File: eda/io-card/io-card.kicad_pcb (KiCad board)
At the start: 2 copper layers, 158 x 95 mm, 63 parts, among them J2 Bus expansion, J3 PortA, J4 PortB, J5 ControlLines, J6 SPI, J7 Keyboard connector, J8 SD-Card module, J9 SD_Card, U1 W65C22SxP, U10 74HCT193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

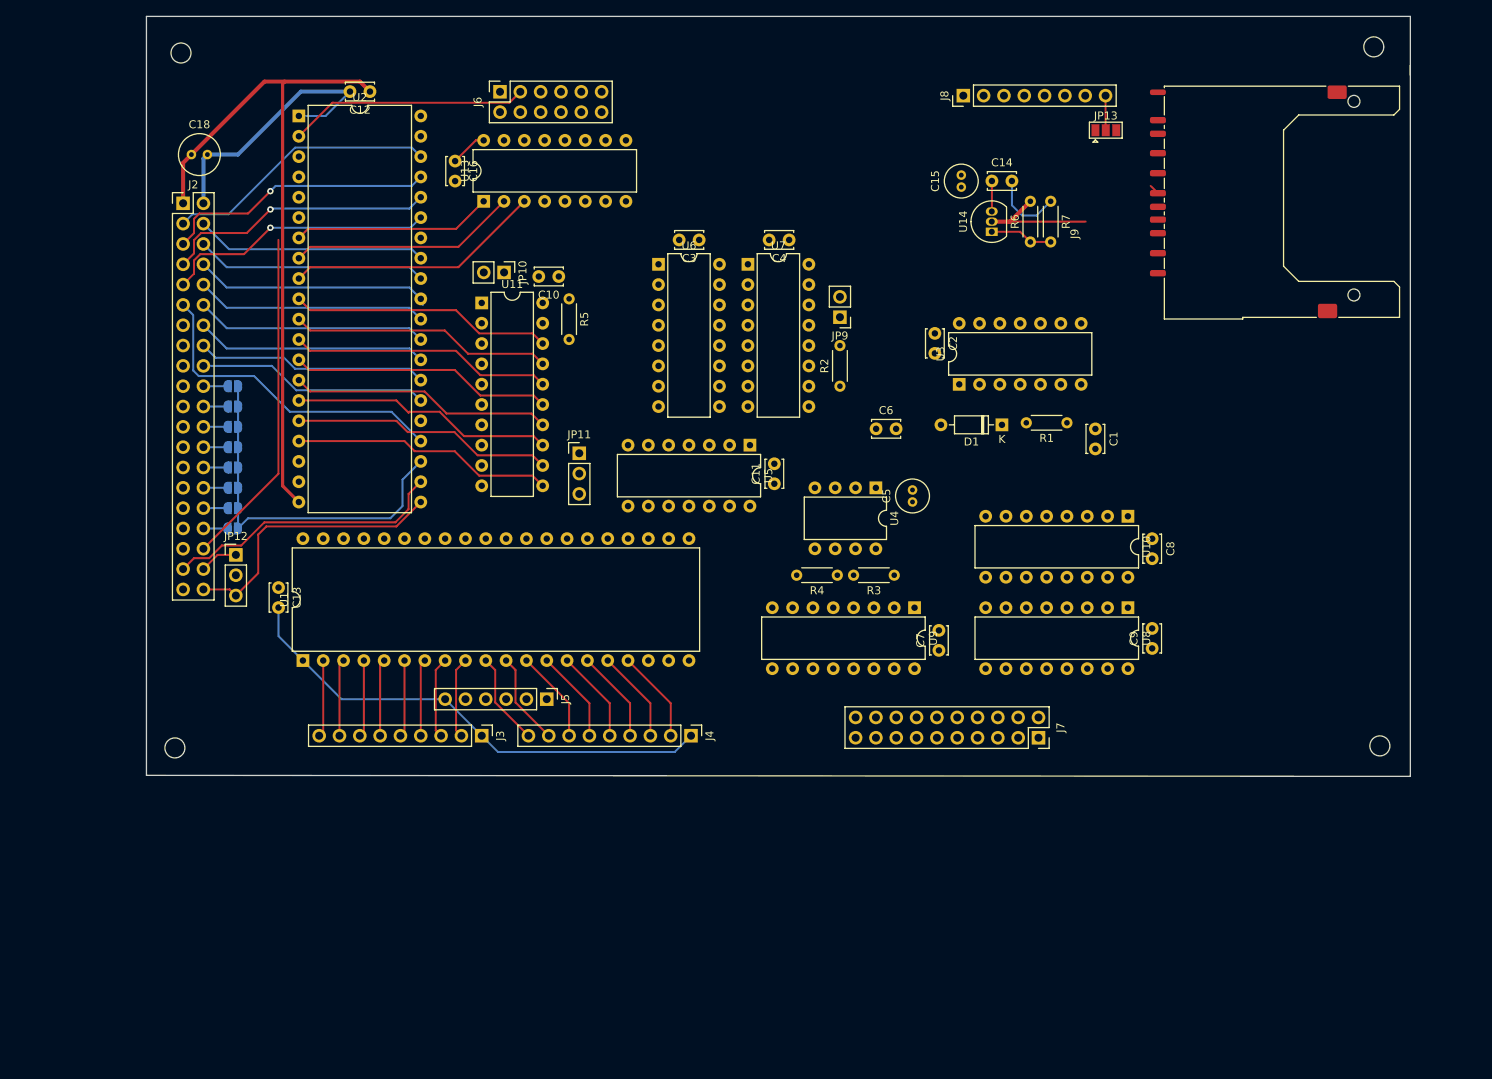
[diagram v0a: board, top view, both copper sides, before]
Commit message: Add skeleton stuff to io-card and gpu
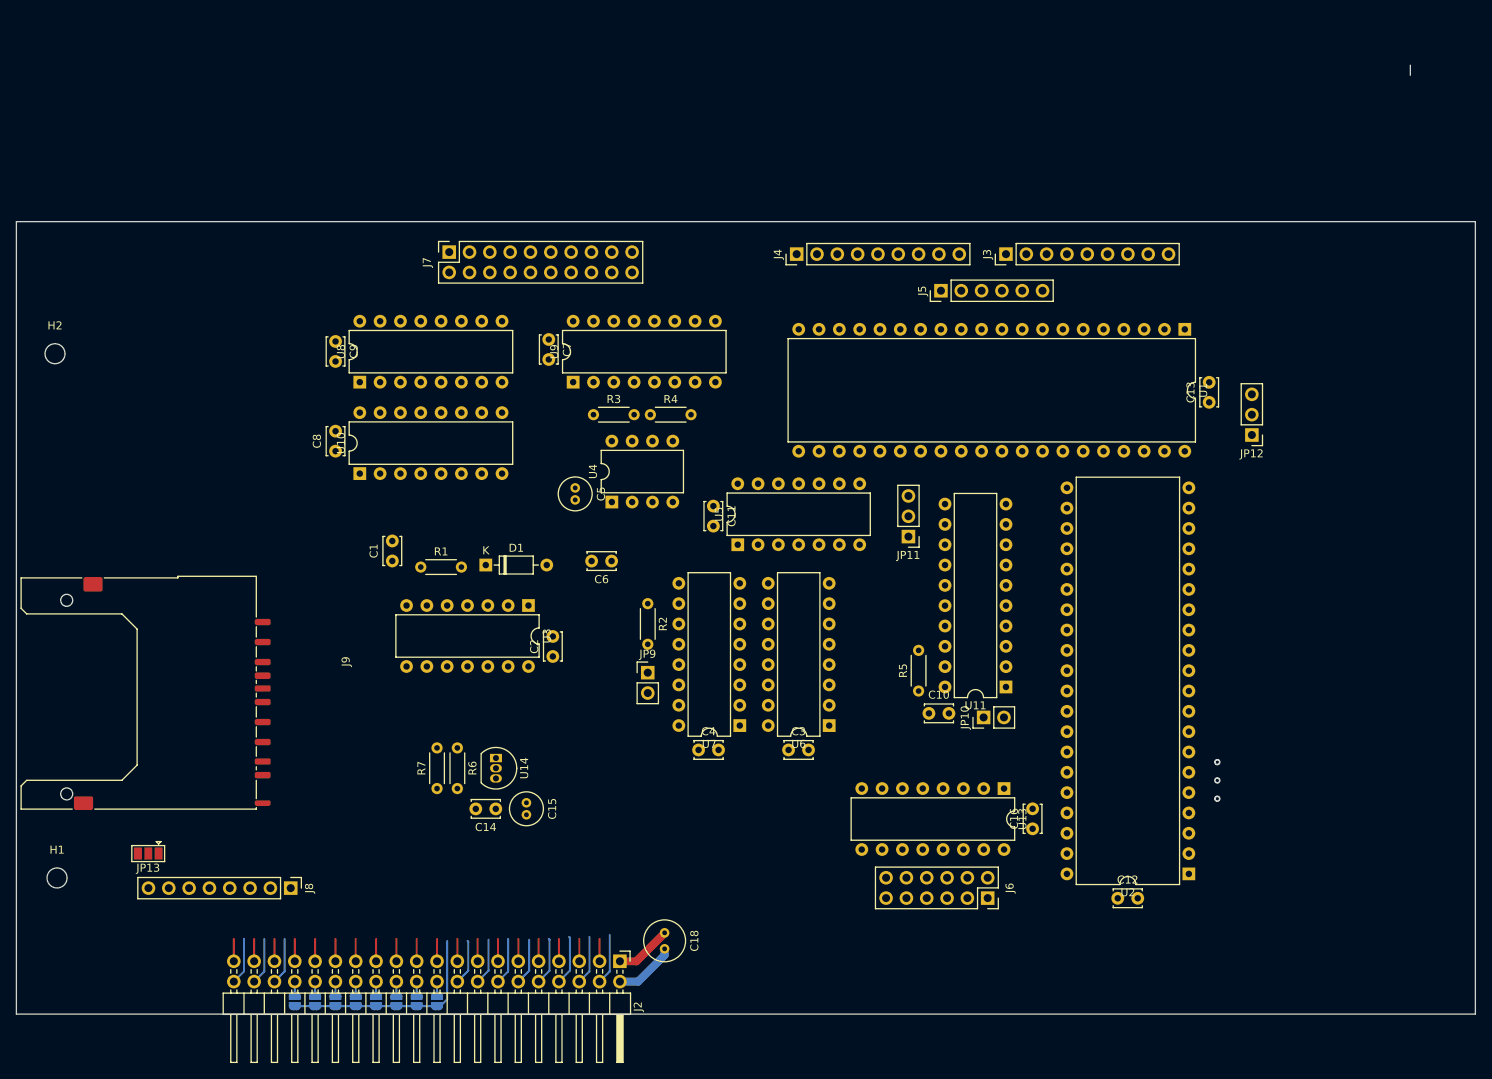
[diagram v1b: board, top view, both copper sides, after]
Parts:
- removed H3, H4: MountingHole, MountingHole:MountingHole_2.5mm
- J2: footprint Connector_PinHeader_2.54mm:PinHeader_2x20_P2.54mm_Vertical -> Connector_PinHeader_2.54mm:PinHeader_2x20_P2.54mm_Horizontal
- moved H2 169.2 mm to (42.4, 71.9)
- moved J9 150.4 mm to (55.9, 114.8), turned to -90 degrees
- moved JP13 150.0 mm to (54.1, 134.4), turned to 180 degrees
- moved U2 146.1 mm to (184.2, 136.9), turned to 180 degrees
- moved C12 137.5 mm to (175.3, 140.0), turned to 0 degrees
- moved J8 129.9 mm to (71.9, 138.7), turned to -90 degrees
- moved JP12 127.9 mm to (192.0, 82.0), turned to 180 degrees
- moved C13 118.6 mm to (186.7, 78.0), turned to 90 degrees
- moved J6 117.8 mm to (159.0, 139.9), turned to -90 degrees
- moved U1 117.8 mm to (183.6, 68.8), turned to -90 degrees
- moved C18 113.9 mm to (118.6, 144.3), turned to -90 degrees
- moved C16 110.4 mm to (164.6, 131.3), turned to 90 degrees
- moved J2 109.4 mm to (113.0, 147.8), turned to -90 degrees
- moved C9 109.1 mm to (77.5, 70.3), turned to -90 degrees
- moved R7 106.2 mm to (90.2, 126.2), turned to 90 degrees
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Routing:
- net GND: track 106.2 -> 7.72 mm
- net VCC: track 95.1 -> 7.05 mm
- net /Expansion header/A4: track 40.8 -> 2.79 mm
- net /~{RST}: track 42.5 -> 5.86 mm
- net /PS2 keyboard interface/KeyboardBit5: track 32.9 -> 0.00 mm
- net /PS2 keyboard interface/KeyboardBit6: track 32.8 -> 0.00 mm
- net /PS2 keyboard interface/KeyboardBit1: track 32.8 -> 0.00 mm
- net /PS2 keyboard interface/KeyboardBit4: track 32.8 -> 0.00 mm
- net /PS2 keyboard interface/KeyboardBit3: track 32.8 -> 0.00 mm
- net /PS2 keyboard interface/KeyboardBit0: track 32.8 -> 0.00 mm
- net /PS2 keyboard interface/KeyboardBit7: track 32.8 -> 0.00 mm
- net /PS2 keyboard interface/KeyboardBit2: track 32.8 -> 0.00 mm
- net /R~{W}: track 35.3 -> 2.79 mm
- net Net-(U13-A2): track 32.2 -> 0.00 mm
- net /Expansion header/A2: track 34.4 -> 2.79 mm
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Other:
- board size 158 x 95 mm -> 182.4 x 118.6 mm
- board text added: "0"
- board text added: "1"
- board text added: "2"
- board text added: "3"
- board text added: "4"
- board text added: "5"
- board text added: "6"
- board text added: "7"

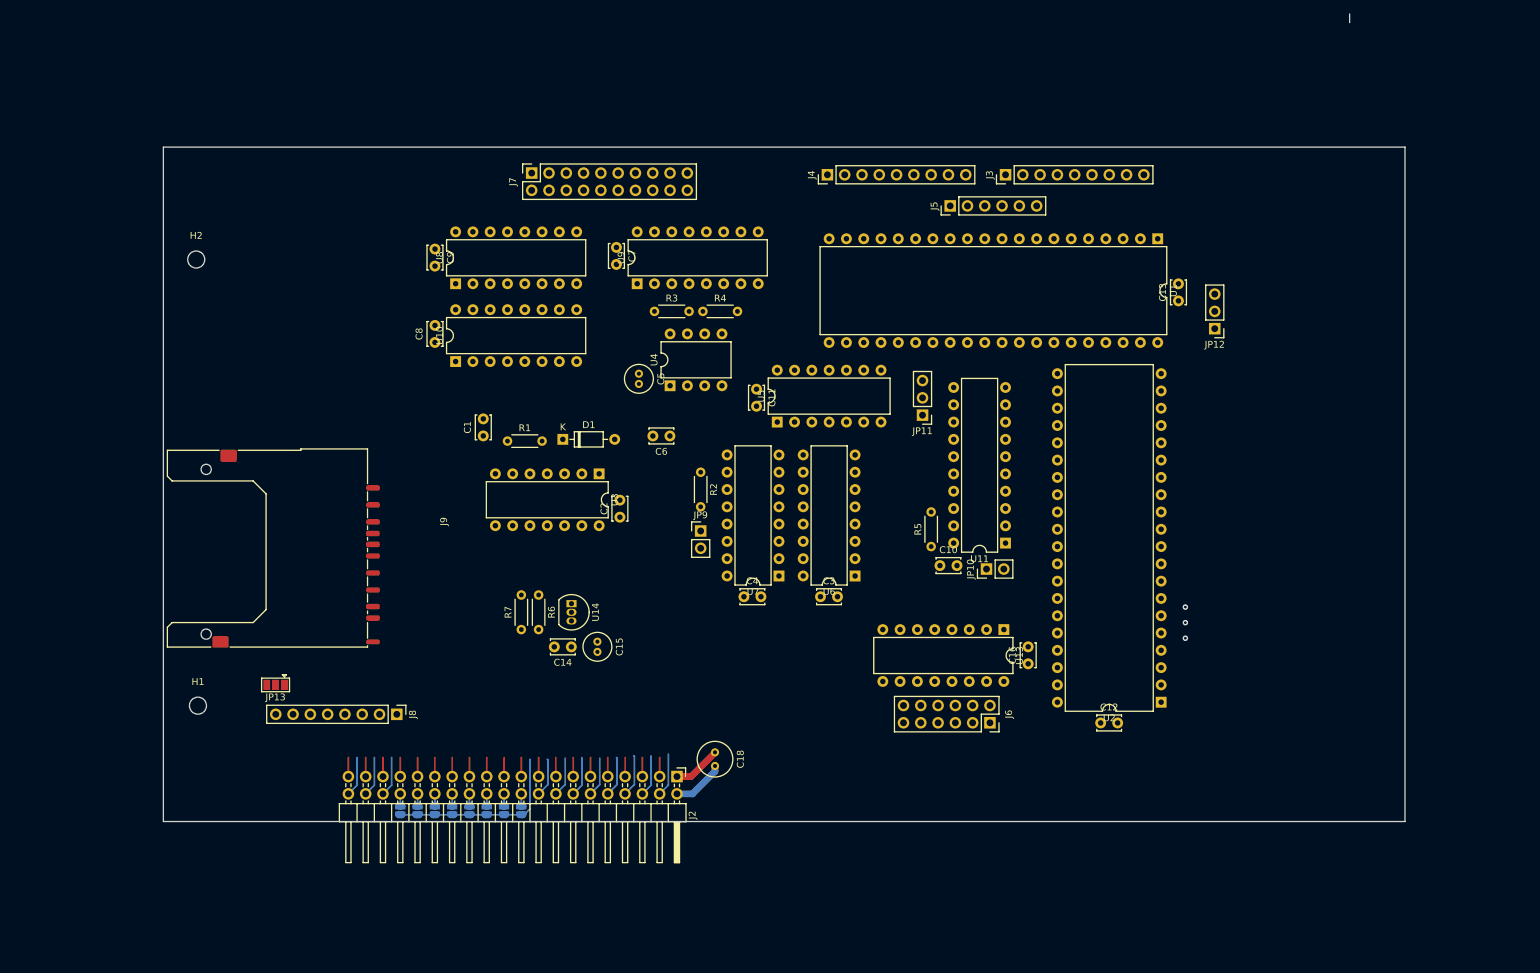
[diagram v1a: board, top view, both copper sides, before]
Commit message: Add expansion backplane
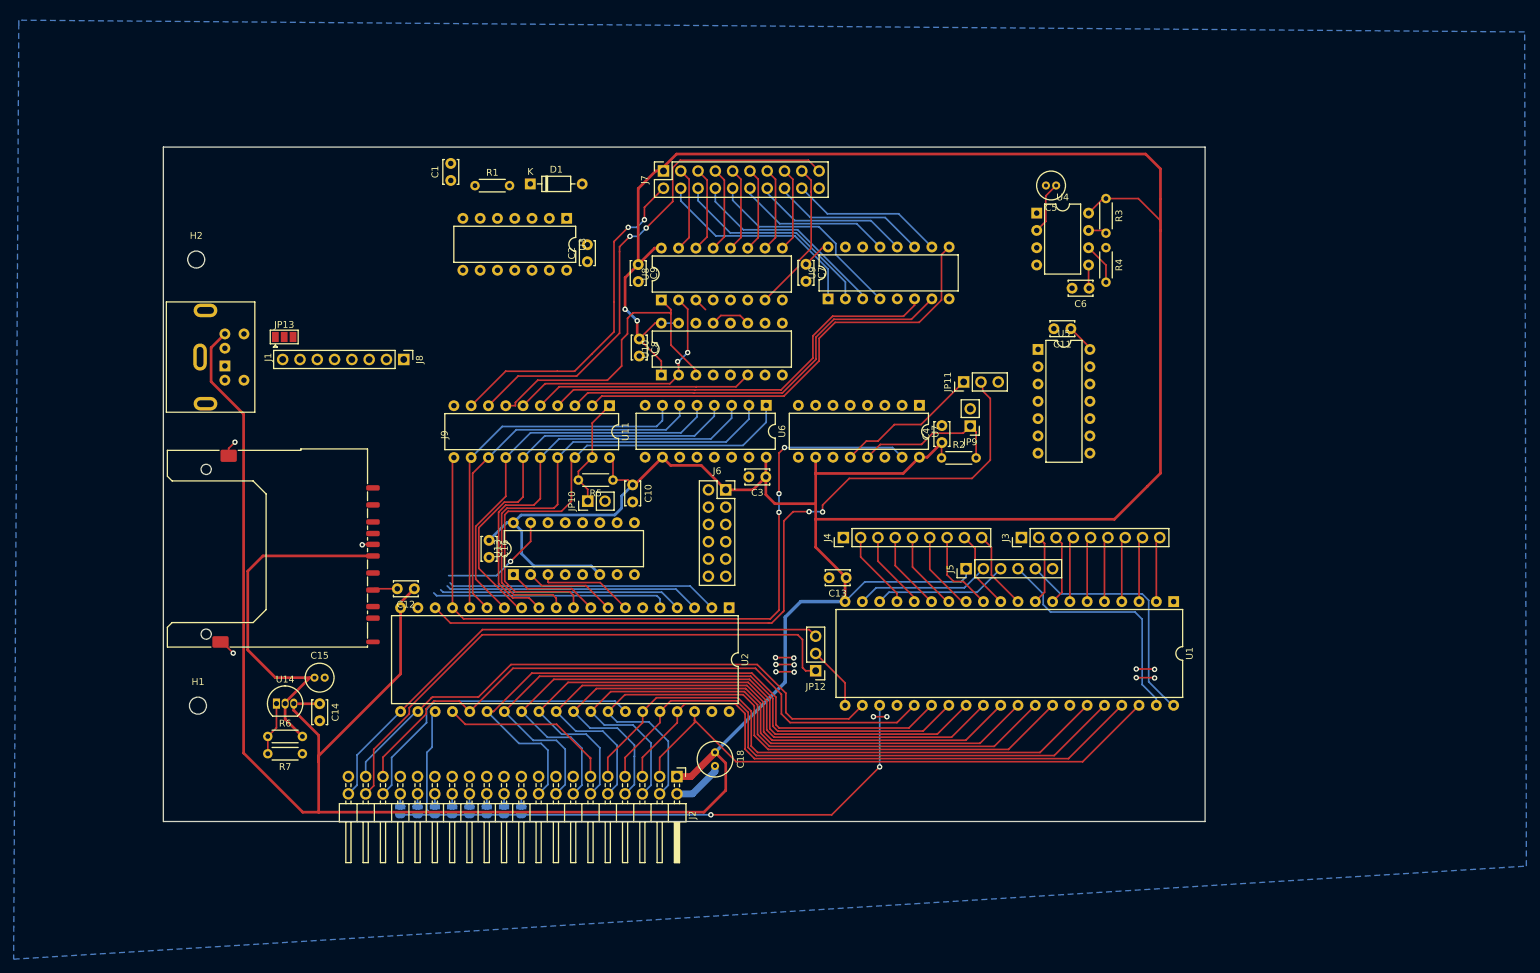
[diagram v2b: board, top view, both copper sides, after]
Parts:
- added J1: PS2, Local:Connector_Mini-DIN_Female_6Pin_2rows, F.Cu at (46.6, 87.5)
- moved C12 102.7 mm to (74.5, 120.2), turned to 180 degrees
- moved C16 81.2 mm to (85.4, 113.1), turned to -90 degrees
- moved JP12 77.2 mm to (133.4, 132.3)
- moved U13 72.5 mm to (89.0, 118.2), turned to 90 degrees
- moved R3 68.4 mm to (176.0, 62.9), turned to -90 degrees
- moved C5 67.2 mm to (168.7, 61.0), turned to 180 degrees
- moved C6 65.3 mm to (173.6, 76.1)
- moved U2 65.0 mm to (120.7, 123.0), turned to -90 degrees
- moved C13 63.5 mm to (137.9, 118.6), turned to 180 degrees
- moved U11 61.6 mm to (103.1, 93.4), turned to -90 degrees
- moved R4 59.9 mm to (176.0, 70.1), turned to -90 degrees
- moved U4 59.5 mm to (165.9, 65.1), turned to 0 degrees
- moved JP10 59.4 mm to (99.9, 107.4)
- moved J5 53.3 mm to (155.5, 117.3)
- moved J3 53.3 mm to (163.6, 112.7)
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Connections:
- U11 pad 2: /Scanning keyboard interface/Scancode0 -> /Scanning keyboard interface/Scancode3
- U11 pad 3: /Scanning keyboard interface/Scancode1 -> /Scanning keyboard interface/Scancode4
- U11 pad 4: /Scanning keyboard interface/Scancode2 -> /Scanning keyboard interface/Scancode5
- U11 pad 5: /Scanning keyboard interface/Scancode3 -> /Scanning keyboard interface/Scancode2
- U11 pad 6: /Scanning keyboard interface/Scancode4 -> /Scanning keyboard interface/Scancode1
- U11 pad 7: /Scanning keyboard interface/Scancode5 -> /Scanning keyboard interface/Scancode0
- U11 pad 8: /Scanning keyboard interface/mod0 -> /Scanning keyboard interface/mod1
- U11 pad 9: /Scanning keyboard interface/mod1 -> /Scanning keyboard interface/mod0
- U2 pad 7: Net-(U13-A0) -> Net-(U13-A2)
- U2 pad 9: Net-(U13-A2) -> Net-(U13-A0)
- U9 pad 1: /Scanning keyboard interface/row4 -> /Scanning keyboard interface/row7
- U9 pad 2: /Scanning keyboard interface/row5 -> /Scanning keyboard interface/row6
- U9 pad 3: /Scanning keyboard interface/row6 -> /Scanning keyboard interface/row5
- U9 pad 4: /Scanning keyboard interface/row7 -> /Scanning keyboard interface/row4
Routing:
- net VCC: track 7.05 -> 636.1 mm, vias 0 -> 2
- net /PS2 keyboard interface/KeyboardBit7: track 0.00 -> 113.7 mm, vias 0 -> 3
- net Net-(JP11-C): track 0.00 -> 112.8 mm, vias 0 -> 2
- net /Clock: track 2.79 -> 94.0 mm
- net /Expansion header/D3: track 5.94 -> 93.6 mm
- net /Expansion header/D0: track 6.37 -> 93.9 mm
- net /Expansion header/D1: track 6.11 -> 93.6 mm
- net /Expansion header/D4: track 5.80 -> 93.3 mm
- net /Expansion header/D2: track 6.19 -> 93.6 mm
- net /Expansion header/D7: track 5.68 -> 93.0 mm
- net /Expansion header/D6: track 5.80 -> 93.1 mm
- net /Expansion header/D5: track 5.86 -> 93.1 mm
- net /Expansion header/A1: track 2.79 -> 87.1 mm, vias 1 -> 0
- net /Expansion header/A2: track 2.79 -> 87.0 mm, vias 1 -> 0
- net /Expansion header/A3: track 2.79 -> 87.0 mm, vias 1 -> 0
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- added copper zone on B.Cu, net GND
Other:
- board size 182.4 x 118.6 mm -> 153 x 99.1 mm
